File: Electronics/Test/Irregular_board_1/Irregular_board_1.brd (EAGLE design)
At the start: 42.9 x 26.7 mm, 9 parts

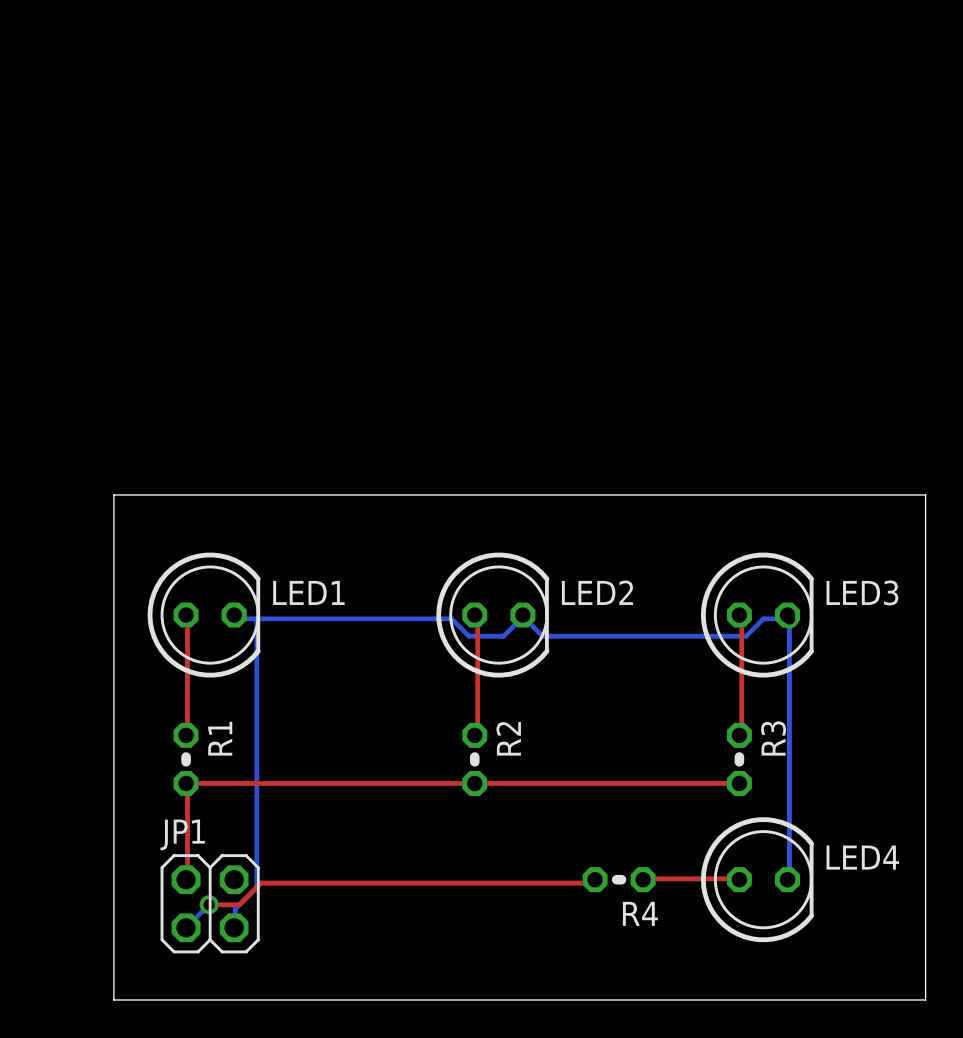
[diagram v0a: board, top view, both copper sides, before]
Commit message: List of parts updated
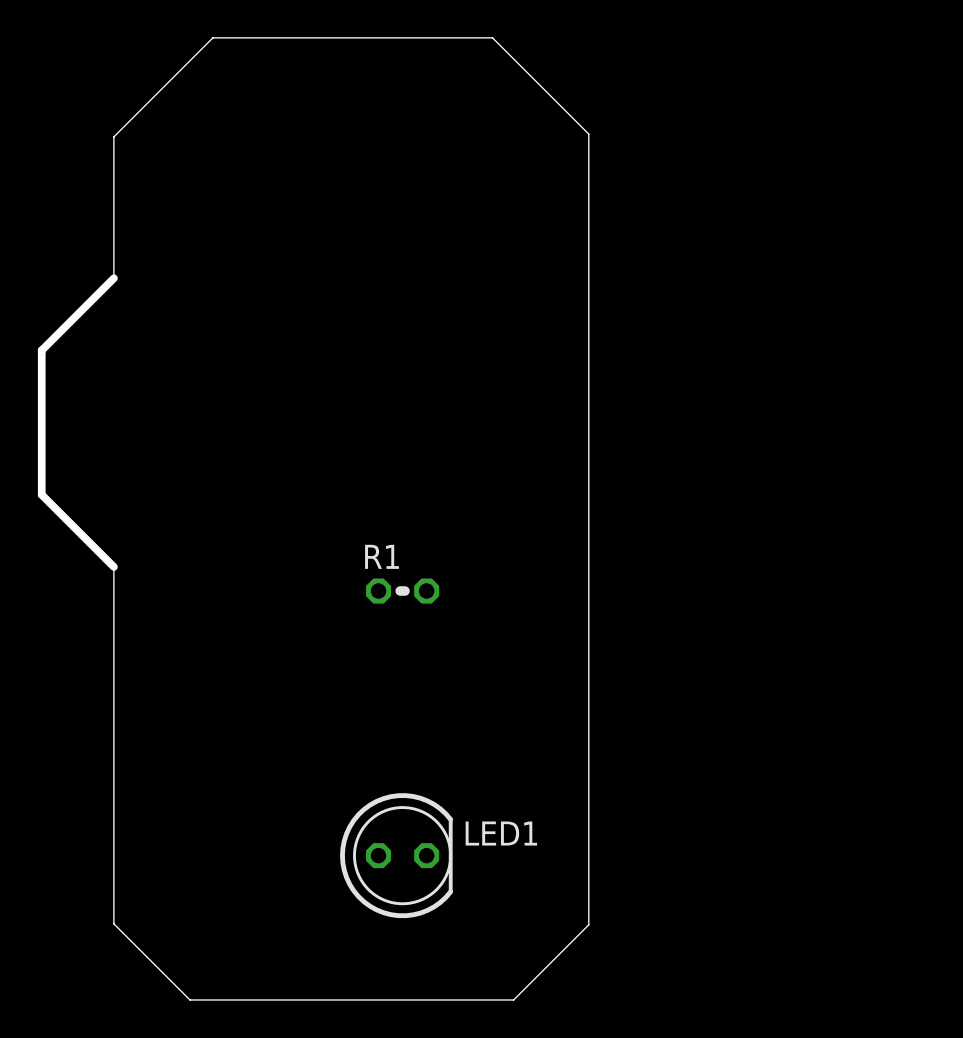
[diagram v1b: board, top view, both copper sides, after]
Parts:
- removed JP1: 2X2, pinhead:2X02
- removed LED2, LED3: 2.58 V, led:LED5MM
- removed LED4: 1.88 V, led:LED5MM
- removed R2, R3: 4K7, resistor:0204V
- removed R4: 1K, resistor:0204V
- LED1: value 2.58 V -> (none)
- R1: value 4K7 -> (none); device resistor:0204V -> rcl:0204V
- moved LED1 16.3 mm to (15.2, 7.62)
- moved R1 14.5 mm to (15.2, 21.6), turned to 0 degrees
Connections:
- removed net N$2: LED2.A, R2.1
- removed net N$3: LED3.A, R3.1
- removed net N$4: LED4.A, R4.1
- removed net N$5: JP1.2, R1.2, R2.2, R3.2
- removed net N$6: JP1.1, R4.2
- removed net N$7: JP1.3, LED1.K, LED2.K, LED3.K, LED4.K
- new net GND: LED1.K
- new net VCC: R1.2
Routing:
- net N$7: track 62.1 -> 0.00 mm, vias 2 -> 0
- net N$5: track 34.3 -> 0.00 mm
- net N$6: track 22.7 -> 0.00 mm, vias 1 -> 0
- net N$2: track 6.45 -> 0.00 mm
- net N$3: track 6.42 -> 0.00 mm
- net N$1: track 6.38 -> 0.00 mm
- net N$4: track 5.10 -> 0.00 mm
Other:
- board size 42.9 x 26.7 mm -> 28.9 x 50.8 mm
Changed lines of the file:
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@@
 <setting verticaltext="up"/>
 </settings>
-<grid distance="0.05" unitdist="inch" unit="inch" style="lines" multiple="1" display="no" altdistance="0.025" altunitdist="inch" altunit="inch"/>
+<grid distance="0.05" unitdist="inch" unit="inch" style="lines" multiple="1" display="yes" altdistance="0.025" altunitdist="inch" altunit="inch"/>
 <layers>
 <layer number="1" name="Top" color="4" fill="1" visible="yes" active="yes"/>
@@
 <layer number="43" name="vRestrict" color="2" fill="10" visible="yes" active="yes"/>
 <layer number="44" name="Drills" color="7" fill="1" visible="no" active="yes"/>
-<layer number="45" name="Holes" color="7" fill="1" visible="yes" active="yes"/>
+<layer number="45" name="Holes" color="7" fill="1" visible="no" active="yes"/>
 <layer number="46" name="Milling" color="3" fill="1" visible="no" active="yes"/>
 <layer number="47" name="Measures" color="7" fill="1" visible="no" active="yes"/>
@@
 <layer number="97" name="Info" color="7" fill="1" visible="no" active="no"/>
 <layer number="98" name="Guide" color="6" fill="1" visible="no" active="no"/>
-<layer number="99" name="SpiceOrder" color="5" fill="1" visible="no" active="no"/>
 </layers>
 <board>
 <plain>
-<wire x1="0" y1="0" x2="42.85" y2="0" width="0" layer="20"/>
-<wire x1="42.85" y1="0" x2="42.85" y2="26.66" width="0" layer="20"/>
-<wire x1="42.85" y1="26.66" x2="0" y2="26.66" width="0" layer="20"/>
-<wire x1="0" y1="26.66" x2="0" y2="0" width="0" layer="20"/>
+<wire x1="0" y1="22.86" x2="0" y2="4.016090625" width="0" layer="20"/>
+<wire x1="0" y1="4.016090625" x2="4.016090625" y2="0" width="0" layer="20"/>
+<wire x1="4.016090625" y1="0" x2="21.10270625" y2="0" width="0" layer="20"/>
+<wire x1="21.10270625" y1="0" x2="25.07" y2="3.96729375" width="0" layer="20"/>
+<wire x1="25.07" y1="3.96729375" x2="25.07" y2="45.709271875" width="0" layer="20"/>
+<wire x1="25.07" y1="45.709271875" x2="19.989271875" y2="50.79" width="0" layer="20"/>
+<wire x1="19.989271875" y1="50.79" x2="5.226640625" y2="50.79" width="0" layer="20"/>
+<wire x1="5.226640625" y1="50.79" x2="0" y2="45.563359375" width="0" layer="20"/>
+<wire x1="0" y1="45.563359375" x2="0" y2="38.1" width="0" layer="20"/>
+<dimension x1="25.07" y1="50.79" x2="0" y2="50.79" x3="12.535" y3="55.88" textsize="1.778" layer="20"/>
+<dimension x1="25.07" y1="0" x2="25.07" y2="50.79" x3="31.75" y3="25.395" textsize="1.778" layer="20"/>
+<wire x1="0" y1="38.1" x2="-3.81" y2="34.29" width="0.4064" layer="20"/>
+<wire x1="-3.81" y1="34.29" x2="-3.81" y2="26.67" width="0.4064" layer="20"/>
+<wire x1="-3.81" y1="26.67" x2="0" y2="22.86" width="0.4064" layer="20"/>
 </plain>
 <attributes>
@@
 </autorouter>
 <elements>
-<element name="JP1" library="pinhead" package="2X02" value="2X2" x="5.08" y="5.08"/>
-<element name="LED1" library="led" package="LED5MM" value="2.58 V" x="5.08" y="20.32">
-<attribute name="CURRENT" value="0.14 mA" x="5.08" y="20.32" size="1.778" layer="27" display="off"/>
-</element>
-<element name="LED2" library="led" package="LED5MM" value="2.58 V" x="20.32" y="20.32">
-<attribute name="CURRENT" value="0.14 mA" x="20.32" y="20.32" size="1.778" layer="27" display="off"/>
-</element>
-<element name="LED3" library="led" package="LED5MM" value="2.58 V" x="34.29" y="20.32">
-<attribute name="CURRENT" value="0.14 mA" x="34.29" y="20.32" size="1.778" layer="27" display="off"/>
-</element>
-<element name="LED4" library="led" package="LED5MM" value="1.88 V" x="34.29" y="6.35">
-<attribute name="CURRENT" value="1.42 mA" x="34.29" y="6.35" size="1.778" layer="27" display="off"/>
-</element>
-<element name="R1" library="resistor" package="0204V" value="4K7" x="3.81" y="12.7" rot="R270"/>
-<element name="R2" library="resistor" package="0204V" value="4K7" x="19.05" y="12.7" rot="R270"/>
-<element name="R3" library="resistor" package="0204V" value="4K7" x="33.02" y="12.7" rot="R270"/>
-<element name="R4" library="resistor" package="0204V" value="1K" x="26.67" y="6.35" rot="R180"/>
+<element name="LED1" library="led" package="LED5MM" value="" x="15.24" y="7.62"/>
+<element name="R1" library="rcl" package="0204V" value="" x="15.24" y="21.59"/>
 </elements>
 <signals>
+<signal name="VCC">
+<contactref element="R1" pad="2"/>
+</signal>
 <signal name="N$1">
 <contactref element="R1" pad="1"/>
 <contactref element="LED1" pad="A"/>
-<wire x1="3.8862" y1="20.1168" x2="3.8862" y2="14.1732" width="0.254" layer="1"/>
-<wire x1="3.8862" y1="14.1732" x2="3.81" y2="13.97" width="0.254" layer="1"/>
-<wire x1="3.8862" y1="20.1168" x2="3.81" y2="20.32" width="0.254" layer="1"/>
+<wire x1="13.97" y1="21.59" x2="13.97" y2="7.62" width="0" layer="19" extent="1-1"/>
 </signal>
-<signal name="N$2">
-<contactref element="R2" pad="1"/>
-<contactref element="LED2" pad="A"/>
-<wire x1="19.2024" y1="20.1168" x2="19.2024" y2="14.1732" width="0.254" layer="1"/>
-<wire x1="19.2024" y1="14.1732" x2="19.05" y2="13.97" width="0.254" layer="1"/>
-<wire x1="19.2024" y1="20.1168" x2="19.05" y2="20.32" width="0.254" layer="1"/>
-</signal>
-<signal name="N$3">
-<contactref element="R3" pad="1"/>
-<contactref element="LED3" pad="A"/>
-<wire x1="33.147" y1="20.1168" x2="33.147" y2="14.1732" width="0.254" layer="1"/>
-<wire x1="33.147" y1="14.1732" x2="33.02" y2="13.97" width="0.254" layer="1"/>
-<wire x1="33.147" y1="20.1168" x2="33.02" y2="20.32" width="0.254" layer="1"/>
-</signal>
-<signal name="N$4">
-<contactref element="R4" pad="1"/>
-<contactref element="LED4" pad="A"/>
-<wire x1="32.9184" y1="6.4008" x2="28.1178" y2="6.4008" width="0.254" layer="1"/>
-<wire x1="28.1178" y1="6.4008" x2="27.94" y2="6.35" width="0.254" layer="1"/>
-<wire x1="32.9184" y1="6.4008" x2="33.02" y2="6.35" width="0.254" layer="1"/>
-</signal>
-<signal name="N$5">
-<contactref element="R1" pad="2"/>
-<contactref element="R2" pad="2"/>
-<contactref element="R3" pad="2"/>
-<contactref element="JP1" pad="2"/>
-<wire x1="3.8862" y1="6.4008" x2="3.8862" y2="11.43" width="0.254" layer="1"/>
-<wire x1="3.8862" y1="6.4008" x2="3.81" y2="6.35" width="0.254" layer="1"/>
-<wire x1="33.02" y1="11.43" x2="19.05" y2="11.43" width="0.254" layer="1"/>
-<wire x1="19.05" y1="11.43" x2="3.8862" y2="11.43" width="0.254" layer="1"/>
-<wire x1="3.8862" y1="11.43" x2="3.81" y2="11.43" width="0.254" layer="1"/>
-</signal>
-<signal name="N$6">
-<contactref element="R4" pad="2"/>
-<contactref element="JP1" pad="1"/>
-<wire x1="7.7724" y1="6.1722" x2="25.3746" y2="6.1722" width="0.254" layer="1"/>
-<wire x1="6.6294" y1="5.0292" x2="7.7724" y2="6.1722" width="0.254" layer="1"/>
-<wire x1="5.0292" y1="5.0292" x2="6.6294" y2="5.0292" width="0.254" layer="1"/>
-<wire x1="3.81" y1="3.81" x2="5.0292" y2="5.0292" width="0.254" layer="16"/>
-<wire x1="25.3746" y1="6.1722" x2="25.4" y2="6.35" width="0.254" layer="1"/>
-<via x="5.0292" y="5.0292" extent="1-16" drill="0.6" shape="square"/>
-</signal>
-<signal name="N$7">
+<signal name="GND">
 <contactref element="LED1" pad="K"/>
-<contactref element="JP1" pad="3"/>
-<contactref element="LED3" pad="K"/>
-<contactref element="LED2" pad="K"/>
-<contactref element="LED4" pad="K"/>
-<wire x1="35.6616" y1="20.1168" x2="35.6616" y2="6.4008" width="0.254" layer="16"/>
-<wire x1="35.6616" y1="6.4008" x2="35.56" y2="6.35" width="0.254" layer="1"/>
-<wire x1="35.6616" y1="20.1168" x2="35.56" y2="20.32" width="0.254" layer="1"/>
-<wire x1="17.8308" y1="20.1168" x2="7.5438" y2="20.1168" width="0.254" layer="16"/>
-<wire x1="7.5438" y1="20.1168" x2="6.4008" y2="20.1168" width="0.254" layer="16"/>
-<wire x1="18.7452" y1="19.2024" x2="17.8308" y2="20.1168" width="0.254" layer="16"/>
-<wire x1="20.574" y1="19.2024" x2="18.7452" y2="19.2024" width="0.254" layer="16"/>
-<wire x1="21.4884" y1="20.1168" x2="20.574" y2="19.2024" width="0.254" layer="16"/>
-<wire x1="6.4008" y1="20.1168" x2="6.35" y2="20.32" width="0.254" layer="16"/>
-<wire x1="21.4884" y1="20.1168" x2="21.59" y2="20.32" width="0.254" layer="16"/>
-<wire x1="6.4008" y1="4.8006" x2="6.4008" y2="3.8862" width="0.254" layer="16"/>
-<wire x1="7.5438" y1="5.9436" x2="6.4008" y2="4.8006" width="0.254" layer="16"/>
-<wire x1="7.5438" y1="20.1168" x2="7.5438" y2="5.9436" width="0.254" layer="16"/>
-<wire x1="6.4008" y1="3.8862" x2="6.35" y2="3.81" width="0.254" layer="16"/>
-<wire x1="34.29" y1="20.1168" x2="35.433" y2="20.1168" width="0.254" layer="16"/>
-<wire x1="33.3756" y1="19.2024" x2="34.29" y2="20.1168" width="0.254" layer="16"/>
-<wire x1="22.6314" y1="19.2024" x2="33.3756" y2="19.2024" width="0.254" layer="16"/>
-<wire x1="21.717" y1="20.1168" x2="22.6314" y2="19.2024" width="0.254" layer="16"/>
-<wire x1="35.433" y1="20.1168" x2="35.56" y2="20.32" width="0.254" layer="16"/>
-<wire x1="21.717" y1="20.1168" x2="21.59" y2="20.32" width="0.254" layer="16"/>
-<via x="35.6616" y="20.1168" extent="1-16" drill="0.6" shape="square"/>
-<via x="35.6616" y="6.4008" extent="1-16" drill="0.6" shape="square"/>
 </signal>
 </signals>
